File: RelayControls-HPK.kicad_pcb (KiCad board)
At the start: 2 copper layers, 180 x 191 mm, 114 parts, among them J1 +, J10 NC, J11 NO, J12 NC, J13 NO, J14 NC, J15 NO, J16 NC, J17 -, J18 COM, J19 COM, J2 -, J20 COM, J21 COM, J22 +, J23 NO, J24 NC, J25 NO, J26 NC, J27 NO, J28 NC, J29 NO, J3 -, J30 NC, J31 -, J32 COM, J33 COM, J34 COM, J35 COM, J36 +, J37 NO, J38 NC, J39 NO, J4 COM, J40 NC, J41 NO, J42 NC, J43 NO, J44 NC, J45 +, J46 -, J5 COM, J6 COM, J7 COM, J8 +, J9 NO, K1 AGQ200A24Z, K2 AGQ200A24Z, K3 AGQ200A24Z, Q1 P_MOS, Q2 P_MOS, Q3 P_MOS

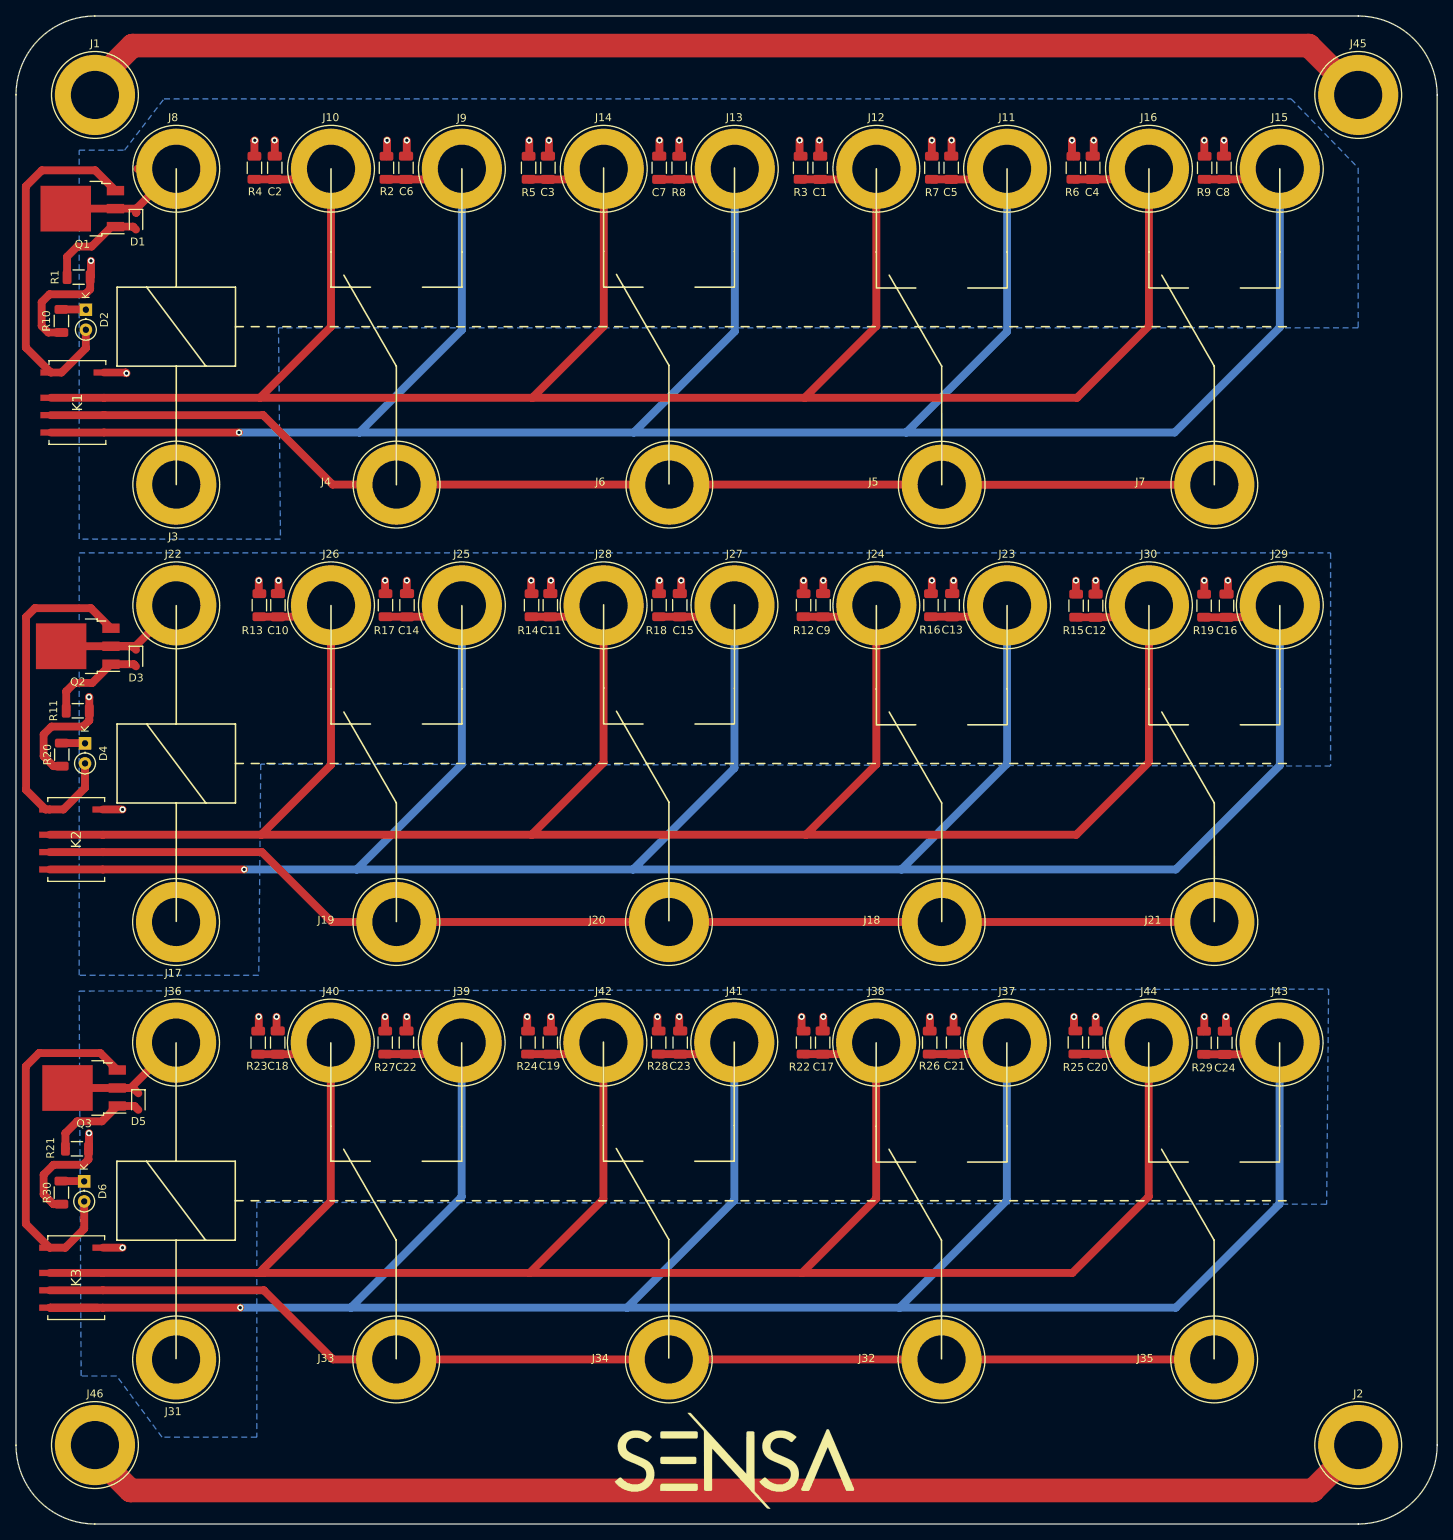
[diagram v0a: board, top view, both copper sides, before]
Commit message: Version 0.1
The width of the PCB has been changed from 180 to 150mm.
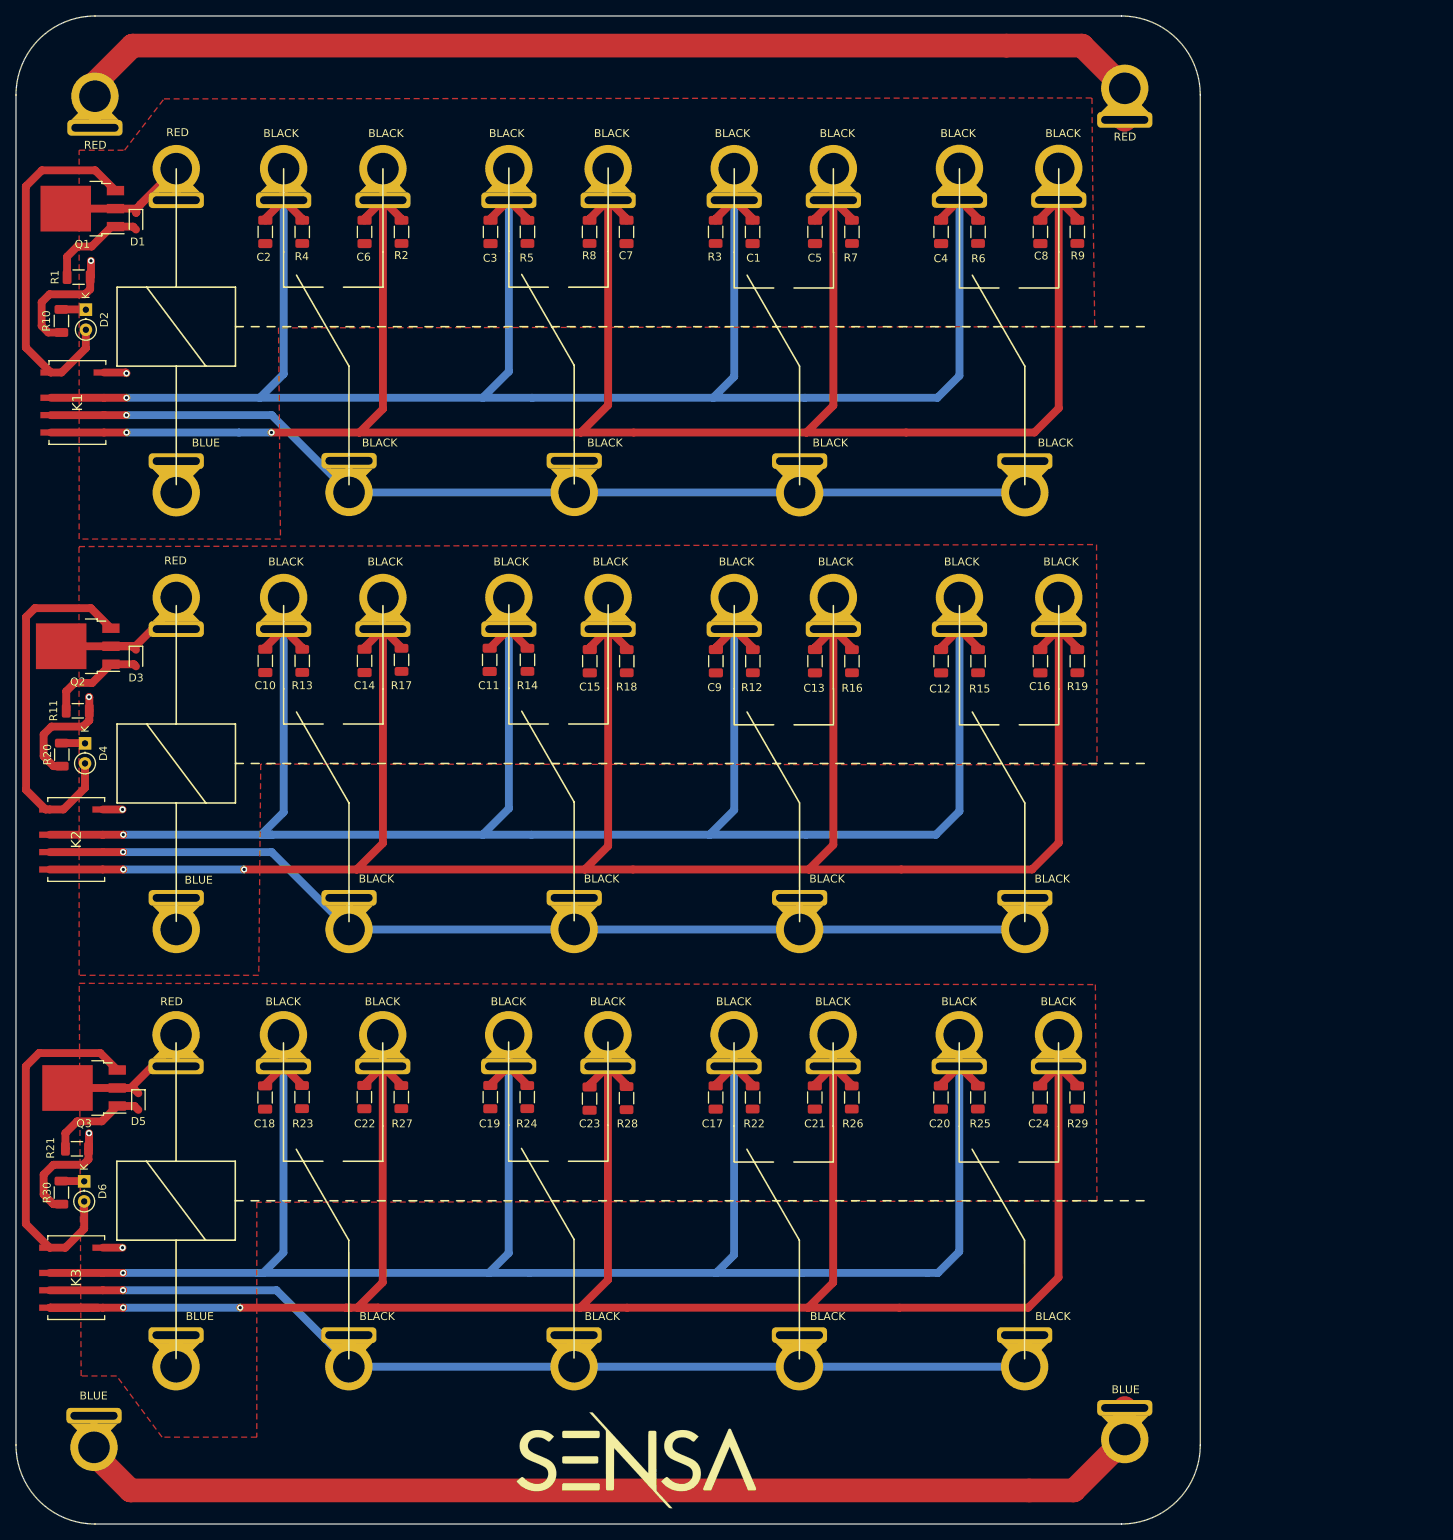
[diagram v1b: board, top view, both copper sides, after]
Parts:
- removed J1, J22, J36, J45, J8: +, Connector:Banana_Jack_1Pin
- removed J10, J12, J14, J16, J24, J26, J28, J30, J38, J40, J42, J44: NC, Connector:Banana_Jack_1Pin
- removed J11, J13, J15, J23, J25, J27, J29, J37, J39, J41, J43, J9: NO, Connector:Banana_Jack_1Pin
- removed J17, J2, J3, J31, J46: -, Connector:Banana_Jack_1Pin
- removed J18, J19, J20, J21, J32, J33, J34, J35, J4, J5, J6, J7: COM, Connector:Banana_Jack_1Pin
- added BLACK: COM, additions:BananaPlug_custom, F.Cu at (60.2, 79.3)
- added BLACK: NC, additions:BananaPlug_custom, F.Cu at (80.4, 38.3)
- added BLACK: NO, additions:BananaPlug_custom, F.Cu at (150.1, 38.3)
- added BLACK: NC, additions:BananaPlug_custom, F.Cu at (137.5, 38.3)
- added BLACK: COM, additions:BananaPlug_custom, F.Cu at (117.3, 134.7)
- added BLACK: COM, additions:BananaPlug_custom, F.Cu at (60.2, 134.7)
- added BLACK: COM, additions:BananaPlug_custom, F.Cu at (88.7, 134.7)
- added BLACK: COM, additions:BananaPlug_custom, F.Cu at (145.8, 134.7)
- added BLACK: NO, additions:BananaPlug_custom, F.Cu at (121.5, 92.7)
- added BLACK: NC, additions:BananaPlug_custom, F.Cu at (109.0, 92.7)
- added BLACK: NO, additions:BananaPlug_custom, F.Cu at (64.5, 92.7)
- added BLACK: COM, additions:BananaPlug_custom, F.Cu at (117.3, 79.4)
- added BLACK: NC, additions:BananaPlug_custom, F.Cu at (51.9, 92.7)
- added BLACK: NO, additions:BananaPlug_custom, F.Cu at (93.0, 92.7)
- added BLACK: NC, additions:BananaPlug_custom, F.Cu at (80.4, 92.7)
- added BLACK: NO, additions:BananaPlug_custom, F.Cu at (150.1, 92.7)
- added BLACK: NC, additions:BananaPlug_custom, F.Cu at (137.5, 92.7)
- added BLACK: COM, additions:BananaPlug_custom, F.Cu at (117.2, 190.1)
- added BLACK: COM, additions:BananaPlug_custom, F.Cu at (60.2, 190.1)
- added BLACK: COM, additions:BananaPlug_custom, F.Cu at (88.7, 190.1)
- added BLACK: COM, additions:BananaPlug_custom, F.Cu at (145.8, 190.1)
- added BLACK: NO, additions:BananaPlug_custom, F.Cu at (121.5, 148.0)
- added BLACK: COM, additions:BananaPlug_custom, F.Cu at (88.7, 79.3)
- added BLACK: NC, additions:BananaPlug_custom, F.Cu at (108.9, 148.0)
- added BLACK: NO, additions:BananaPlug_custom, F.Cu at (64.5, 148.0)
- added BLACK: NC, additions:BananaPlug_custom, F.Cu at (51.9, 148.0)
- added BLACK: NO, additions:BananaPlug_custom, F.Cu at (93.0, 148.0)
- added BLACK: NC, additions:BananaPlug_custom, F.Cu at (80.4, 148.0)
- added BLACK: NO, additions:BananaPlug_custom, F.Cu at (150.0, 148.0)
- added BLACK: NC, additions:BananaPlug_custom, F.Cu at (137.5, 148.0)
- added BLACK: COM, additions:BananaPlug_custom, F.Cu at (145.8, 79.4)
- added BLACK: NO, additions:BananaPlug_custom, F.Cu at (64.5, 38.3)
- added BLACK: NC, additions:BananaPlug_custom, F.Cu at (51.9, 38.3)
- added BLACK: NO, additions:BananaPlug_custom, F.Cu at (121.5, 38.3)
- added BLACK: NC, additions:BananaPlug_custom, F.Cu at (109.0, 38.3)
- added BLACK: NO, additions:BananaPlug_custom, F.Cu at (93.0, 38.3)
- added BLUE: -, additions:BananaPlug_custom, F.Cu at (27.9, 200.3)
- added BLUE: -, additions:BananaPlug_custom, F.Cu at (38.3, 79.4)
- added BLUE: -, additions:BananaPlug_custom, F.Cu at (38.3, 134.7)
- added BLUE: -, additions:BananaPlug_custom, F.Cu at (38.3, 190.1)
- added BLUE: -, additions:BananaPlug_custom, F.Cu at (158.4, 199.3)
- added RED: +, additions:BananaPlug_custom, F.Cu at (28.0, 29.2)
- added RED: +, additions:BananaPlug_custom, F.Cu at (38.3, 38.3)
- added RED: +, additions:BananaPlug_custom, F.Cu at (38.3, 92.7)
- added RED: +, additions:BananaPlug_custom, F.Cu at (38.3, 148.0)
- added RED: +, additions:BananaPlug_custom, F.Cu at (158.4, 28.2)
- moved C8 24.6 mm to (147.7, 46.4), turned to 90 degrees
- moved C16 24.6 mm to (147.7, 100.7), turned to 90 degrees
- moved C24 24.4 mm to (147.7, 156.0), turned to 90 degrees
- moved C4 20.9 mm to (135.2, 46.4), turned to 270 degrees
- moved C20 20.8 mm to (135.1, 156.0), turned to 270 degrees
- moved C12 20.8 mm to (135.2, 100.7), turned to 270 degrees
- moved C5 19.1 mm to (119.2, 46.4), turned to 90 degrees
- moved C21 18.9 mm to (119.2, 156.0), turned to 90 degrees
- moved C13 18.8 mm to (119.2, 100.7), turned to 90 degrees
- moved R9 18.1 mm to (152.4, 46.4), turned to 90 degrees
- moved R19 17.5 mm to (152.4, 100.7), turned to 90 degrees
- moved R29 17.5 mm to (152.4, 156.0), turned to 90 degrees
- moved G*** 15.5 mm to (90.8, 114.5)
- moved C9 15.3 mm to (106.6, 100.7), turned to 270 degrees
- moved C17 15.2 mm to (106.6, 156.0), turned to 270 degrees
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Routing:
- net NO1: track 337.8 -> 291.9 mm, vias 1 -> 2
- net NC3: track 309.0 -> 265.0 mm, vias 0 -> 1
- net NO2: track 339.2 -> 295.8 mm, vias 1 -> 2
- net NO3: track 346.6 -> 304.9 mm, vias 1 -> 2
- net NC1: track 301.6 -> 261.5 mm, vias 0 -> 1
- net NC2: track 300.3 -> 269.2 mm, vias 0 -> 1
- net R1-: track 51.8 -> 23.2 mm, vias 18 -> 2
- net R3-: track 47.1 -> 21.6 mm, vias 18 -> 2
- net R2-: track 44.8 -> 21.6 mm, vias 18 -> 2
- net Net-(J1-Pad1): track 166.1 -> 144.1 mm
- net Net-(J2-Pad1): track 165.5 -> 144.2 mm
- net Net-(D1-Pad1): track 21.7 -> 31.1 mm
- net COM2: track 151.2 -> 143.6 mm, vias 0 -> 1
- net COM1: track 151.0 -> 143.4 mm, vias 0 -> 1
- net COM3: track 151.1 -> 143.8 mm, vias 0 -> 1
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- added copper zone on F.Cu, net R1-
- added copper zone on F.Cu, net R2-
- added copper zone on F.Cu, net R3-
- removed copper zone on B.Cu, net R1-
- removed copper zone on B.Cu, net R2-
- removed copper zone on B.Cu, net R3-
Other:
- board size 180 x 191 mm -> 150 x 191 mm

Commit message: Reverse polarity protection
Fixed the reverse polarity protection.
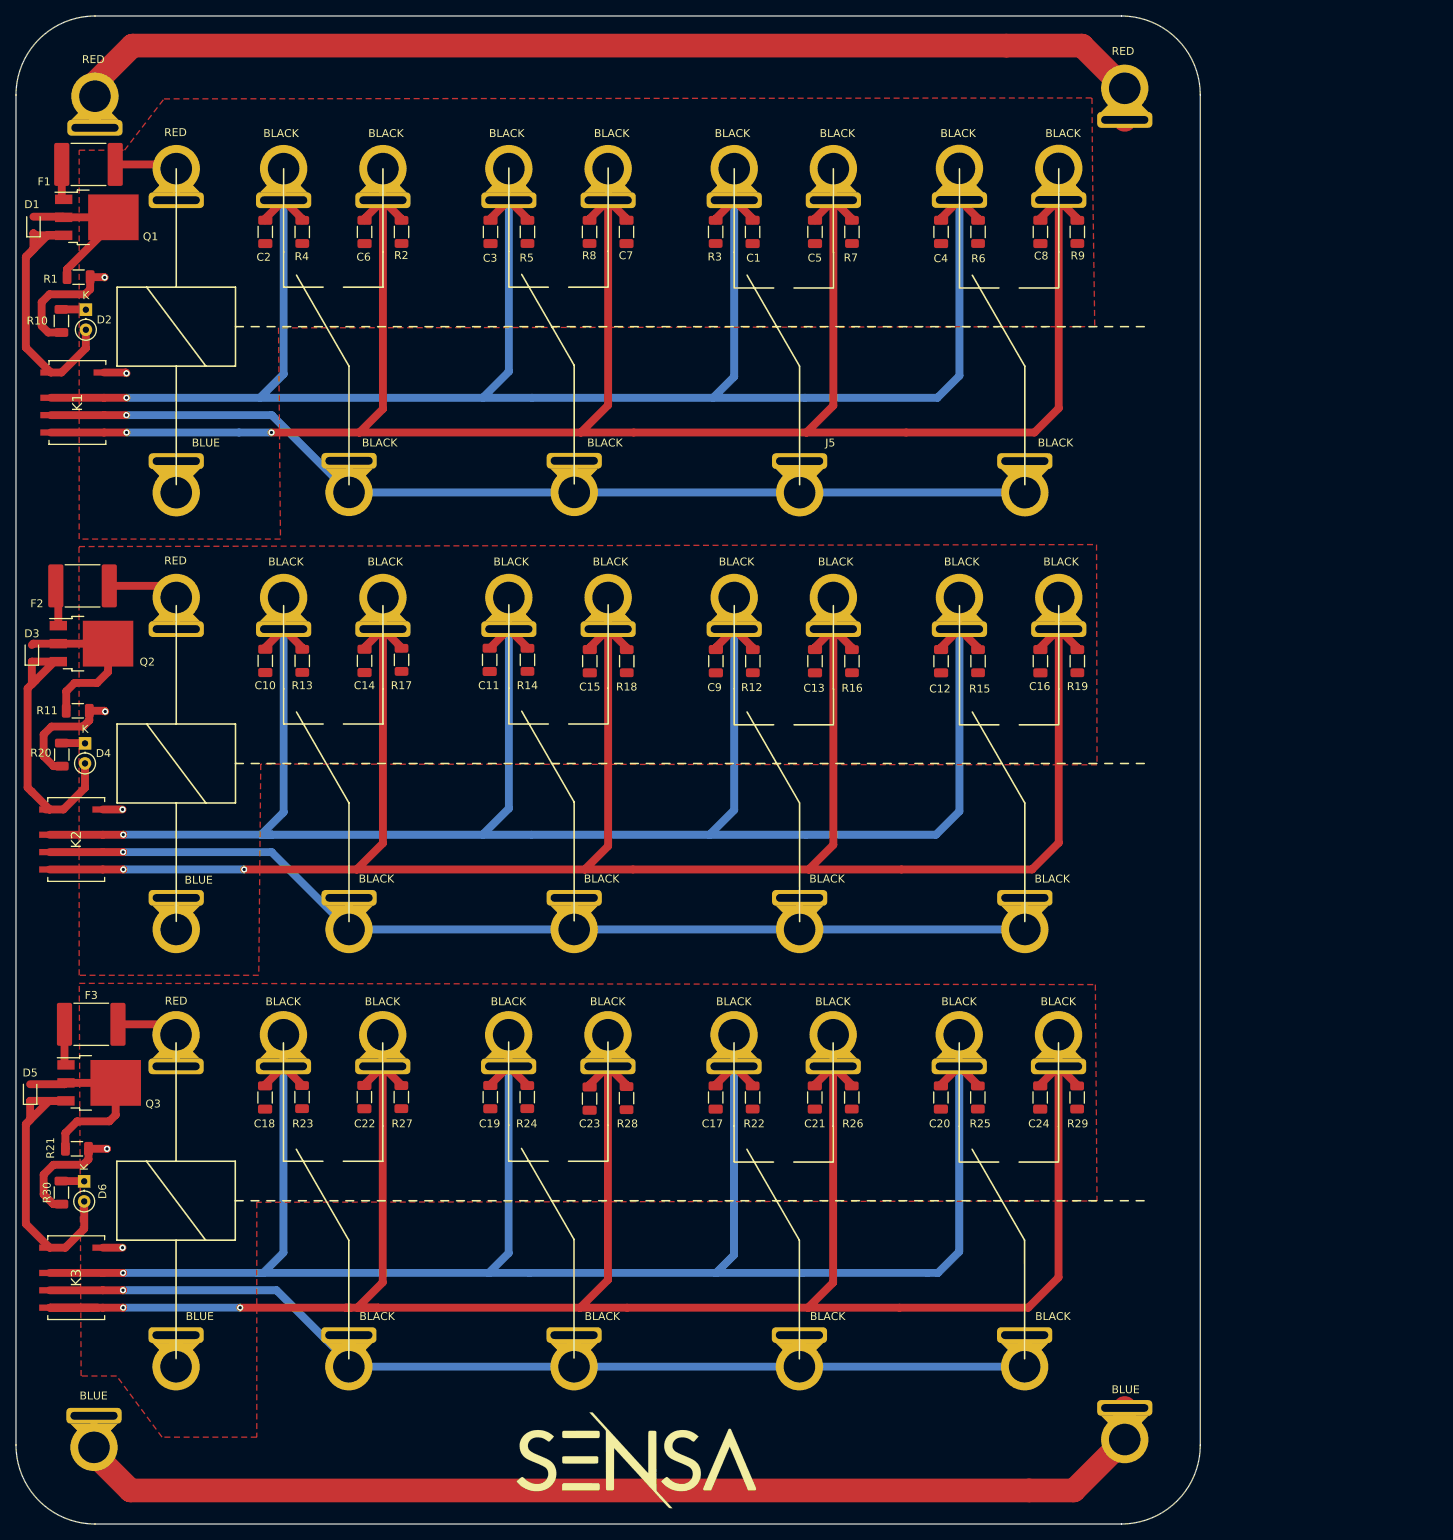
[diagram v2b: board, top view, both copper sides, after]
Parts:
- added F1: Fuse, Fuse:Fuse_2920_7451Metric, F.Cu at (27.2, 37.8)
- added F2: Fuse, Fuse:Fuse_2920_7451Metric, F.Cu at (26.4, 91.2)
- added F3: Fuse, Fuse:Fuse_2920_7451Metric, F.Cu at (27.5, 146.7)
- Q1, Q2, Q3: value P_MOS -> BS250
- R1, R11, R21: value 100K -> 10K
- moved D5 13.8 mm to (19.8, 155.3), turned to 90 degrees
- moved D3 13.2 mm to (20.0, 99.7), turned to 90 degrees
- moved D1 13.0 mm to (20.2, 45.5), turned to 90 degrees
- moved Q1 2.14 mm to (28.2, 44.5), turned to 0 degrees
- moved Q3 2.01 mm to (28.5, 154.1), turned to 0 degrees
- moved Q2 1.77 mm to (27.6, 98.5), turned to 0 degrees
- renumbered BLACK to J5
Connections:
- D1 pad 1: Net-(D1-Pad1) -> R1+
- D3 pad 1: Net-(D3-Pad1) -> R2+
- D5 pad 1: Net-(D5-Pad1) -> R3+
- Q1 pad 1: Net-(D1-Pad2) -> Net-(F1-Pad1)
- Q1 pad 2: Net-(D1-Pad1) -> Net-(D1-Pad2)
- Q2 pad 1: Net-(D3-Pad2) -> Net-(F2-Pad1)
- Q2 pad 2: Net-(D3-Pad1) -> Net-(D3-Pad2)
- Q3 pad 1: Net-(D5-Pad2) -> Net-(F3-Pad1)
- Q3 pad 2: Net-(D5-Pad1) -> Net-(D5-Pad2)
- RED pad 1: Net-(D1-Pad1) -> Net-(F1-Pad2)
- RED pad 1: Net-(D3-Pad1) -> Net-(F2-Pad2)
- RED pad 1: Net-(D5-Pad1) -> Net-(F3-Pad2)
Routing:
- net Net-(D1-Pad1): track 31.1 -> 0.00 mm
- net Net-(D3-Pad1): track 24.1 -> 0.00 mm
- net Net-(D5-Pad1): track 23.1 -> 0.00 mm
- net Net-(F1-Pad2): track 0.00 -> 18.2 mm
- net Net-(F2-Pad2): track 0.00 -> 13.1 mm
- net Net-(F3-Pad2): track 0.00 -> 11.9 mm
- net Net-(D5-Pad2): track 12.9 -> 24.3 mm
- net Net-(D3-Pad2): track 12.8 -> 22.1 mm
- net R2+: track 46.9 -> 37.9 mm
- net R1+: track 46.2 -> 37.3 mm
- net R3+: track 46.2 -> 39.8 mm
- net Net-(F3-Pad1): track 0.00 -> 5.22 mm
- net Net-(F2-Pad1): track 0.00 -> 5.17 mm
- net Net-(D1-Pad2): track 13.0 -> 17.7 mm
- net Net-(F1-Pad1): track 0.00 -> 4.52 mm

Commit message: Edits
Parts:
- added G***: LOGO, additions:QRcode_Smaller, B.Cu at (90.9, 168.3)
